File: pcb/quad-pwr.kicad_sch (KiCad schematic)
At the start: 18 parts, among them U3 MAX20029

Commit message: dogbone for ddr
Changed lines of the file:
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@@
 	)
 	(junction
+		(at 114.3 104.14)
+		(diameter 0)
+		(color 0 0 0 0)
+	)
+	(junction
 		(at 81.28 73.66)
 		(diameter 0)
@@
 	(wire
 		(pts
+			(xy 114.3 104.14) (xy 142.24 104.14)
+		)
+		(stroke
+			(width 0)
+			(type default)
+		)
+	)
+	(wire
+		(pts
 			(xy 193.04 86.36) (xy 213.36 86.36)
 		)
@@
 	(wire
 		(pts
+			(xy 114.3 134.62) (xy 238.76 134.62)
+		)
+		(stroke
+			(width 0)
+			(type default)
+		)
+	)
+	(wire
+		(pts
 			(xy 71.12 101.6) (xy 71.12 83.82)
 		)
@@
 	(wire
 		(pts
-			(xy 60.96 104.14) (xy 142.24 104.14)
+			(xy 60.96 104.14) (xy 114.3 104.14)
 		)
 		(stroke
@@
 	(wire
 		(pts
+			(xy 114.3 104.14) (xy 114.3 134.62)
+		)
+		(stroke
+			(width 0)
+			(type default)
+		)
+	)
+	(wire
+		(pts
 			(xy 71.12 101.6) (xy 142.24 101.6)
 		)
@@
 		)
 	)
+	(label "3V3_PG"
+		(at 236.22 134.62 180)
+		(effects
+			(font
+				(size 1.27 1.27)
+			)
+			(justify right bottom)
+		)
+	)
 	(label "3V3_FD"
 		(at 233.68 96.52 180)
@@
 		)
 	)
+	(hierarchical_label "3V3_PG"
+		(shape output)
+		(at 238.76 134.62 0)
+		(effects
+			(font
+				(size 1.27 1.27)
+			)
+			(justify left)
+		)
+	)

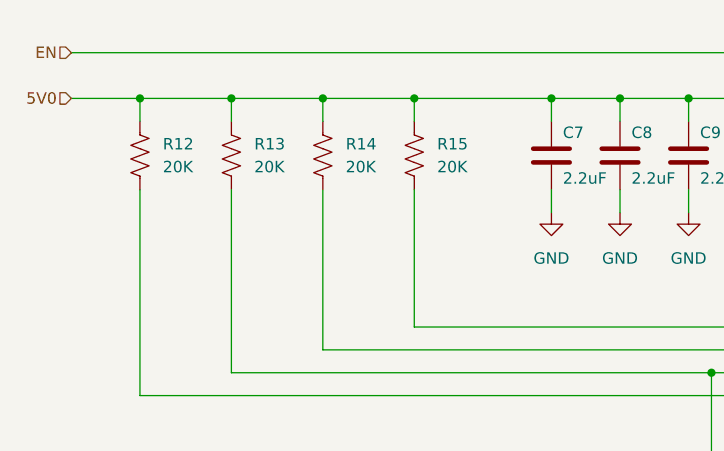
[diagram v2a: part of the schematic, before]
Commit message: added jlc fab
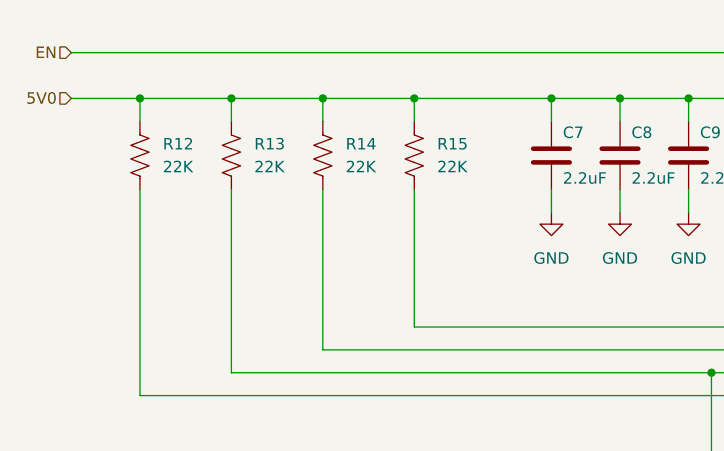
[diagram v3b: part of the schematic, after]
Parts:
- R12, R13, R14, R15: value 20K -> 22K
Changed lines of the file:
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@@
 			)
 		)
-		(property "Value" "20K"
+		(property "Value" "22K"
 			(at 63.5 81.2799 0)
 			(show_name no)
@@
 			)
 		)
-		(property "Value" "20K"
+		(property "Value" "22K"
 			(at 73.66 81.2799 0)
 			(show_name no)
@@
 			)
 		)
-		(property "Value" "20K"
+		(property "Value" "22K"
 			(at 83.82 81.2799 0)
 			(show_name no)
@@
 			)
 		)
-		(property "Value" "20K"
+		(property "Value" "22K"
 			(at 53.34 81.2799 0)
 			(show_name no)
